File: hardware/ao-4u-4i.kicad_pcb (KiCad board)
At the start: 4 copper layers, 100 x 85 mm, 225 parts, among them J101 TNG-Power-TOP, J102 TNG-Power-BTM, J103 TNG-Data-TOP, J104 TNG-Data-BTM, P102 Debug, P103 PE, P201 INPUT0, P202 INPUT1, P203 INPUT2, P204 INPUT3, Q101 FDS8449, SW101 BOOT, T101 744273222, U101 STM32F070CBT6, U102 AZ1117EH, U103 82400152, U104 TEL10, U105 TLP293, U106 STEF01, U201 DAC8760, U202 DAC8760, U203 ISO7741DWR, U204 DAC8760, U205 DAC8760, U206 TPS560430YDBVR, U207 TPS7A3001DGNR, U208 TPS7A4901DGNR, U209 LTC3261, X101 TBD

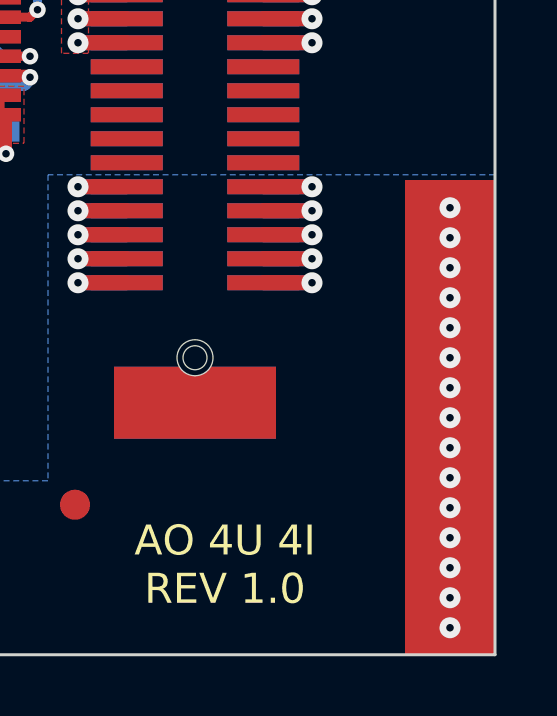
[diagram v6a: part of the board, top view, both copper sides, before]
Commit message: add hook footprint
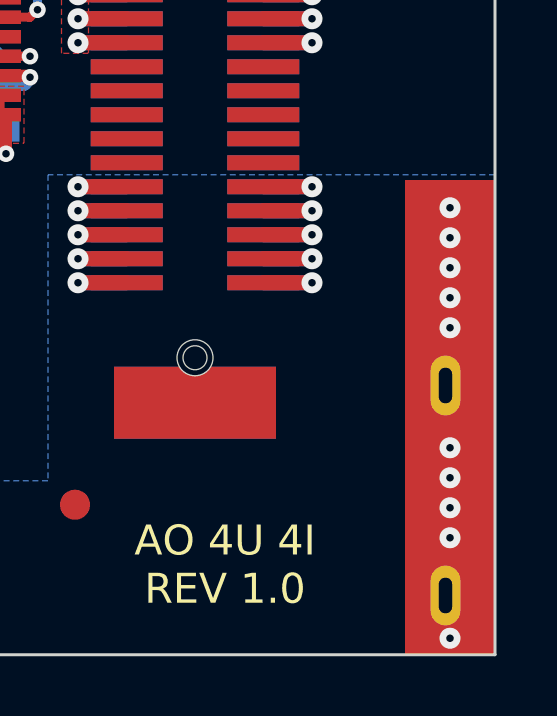
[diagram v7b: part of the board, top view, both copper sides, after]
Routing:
- net Earth: track 54.1 -> 54.5 mm, vias 31 -> 26
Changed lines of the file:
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@@
     (thickness 1.6)
     (drawings 29)
-    (tracks 3141)
+    (tracks 3136)
     (zones 0)
     (modules 225)
@@
     (add_net USB-DPC)
   )
+  (module kicad-libraries:PE_Hook (layer F.Cu)
+    (at 188.3 139.6)
+    (fp_text reference P103 (at 0 0.5) (layer F.Fab)
+      (effects (font (size 0.15 0.15) (thickness 0.0375)))
+    )
+    (fp_text value PE (at 0 -0.5) (layer F.Fab)
+      (effects (font (size 0.15 0.15) (thickness 0.0375)))
+    )
+    (pad 1 thru_hole oval (at -0.15 -1.075) (size 1 2) (drill oval 0.45 1.2) (layers *.Cu *.Mask)
+      (net 12 Earth))
+    (pad 1 thru_hole oval (at -0.15 5.925) (size 1 2) (drill oval 0.45 1.2) (layers *.Cu *.Mask)
+      (net 12 Earth))
+    (pad 1 smd rect (at 0 0) (size 3 15.85) (layers F.Cu)
+      (net 12 Earth))
+    (model Connectors_TF/PE_Hook.wrl
+      (at (xyz 0 0 0))
+      (scale (xyz 1 1 1))
+      (rotate (xyz 0 0 0))
+    )
+  )
   (module LED-LP (layer B.Cu)
     (at 101.4 109 90)
@@
       (clearance 0.65024))
   )
-  (module kicad-libraries:PE_Hook (layer F.Cu)
-    (at 188.3 139.6)
-    (fp_text reference P103 (at 0 0.5) (layer F.Fab)
-      (effects (font (size 0.15 0.15) (thickness 0.0375)))
-    )
-    (fp_text value PE (at 0 -0.5) (layer F.Fab)
-      (effects (font (size 0.15 0.15) (thickness 0.0375)))
-    )
-    (pad 1 smd rect (at 0 0) (size 3 15.85) (layers B.Cu B.Paste B.Mask)
-      (net 12 Earth))
-    (pad 1 smd rect (at 0 0) (size 3 15.85) (layers F.Cu F.Paste F.Mask)
-      (net 12 Earth))
-  )
   (module kicad-libraries:TEL10 (layer F.Cu)
     (at 133.15 135.25 180)
@@
   (via (at 175.9 135.1) (size 0.7) (drill 0.25) (layers F.Cu B.Cu) (net 12))
   (segment (start 175.9 135.1) (end 177.525 135.1) (width 0.5) (layer F.Cu) (net 12) (status 800000))
-  (via (at 188.3 139.6) (size 0.7) (drill 0.25) (layers F.Cu B.Cu) (net 12))
-  (via (at 188.3 138.6) (size 0.7) (drill 0.25) (layers F.Cu B.Cu) (net 12))
   (segment (start 188.3 139.6) (end 188.3 138.6) (width 0.7) (layer F.Cu) (net 12))
-  (via (at 188.3 137.6) (size 0.7) (drill 0.25) (layers F.Cu B.Cu) (net 12))
   (segment (start 188.3 139.6) (end 188.3 137.6) (width 0.7) (layer F.Cu) (net 12))
   (via (at 188.3 136.6) (size 0.7) (drill 0.25) (layers F.Cu B.Cu) (net 12))
@@
   (via (at 188.3 143.6) (size 0.7) (drill 0.25) (layers F.Cu B.Cu) (net 12))
   (segment (start 188.3 142.6) (end 188.3 143.6) (width 0.7) (layer B.Cu) (net 12))
-  (via (at 188.3 144.6) (size 0.7) (drill 0.25) (layers F.Cu B.Cu) (net 12))
   (segment (start 188.3 143.6) (end 188.3 144.6) (width 0.7) (layer F.Cu) (net 12))
-  (via (at 188.3 145.6) (size 0.7) (drill 0.25) (layers F.Cu B.Cu) (net 12))
   (segment (start 188.3 144.6) (end 188.3 145.6) (width 0.7) (layer B.Cu) (net 12))
-  (via (at 188.3 146.6) (size 0.7) (drill 0.25) (layers F.Cu B.Cu) (net 12))
-  (segment (start 188.3 145.6) (end 188.3 146.6) (width 0.7) (layer F.Cu) (net 12))
   (via (at 188.3 135.6) (size 0.7) (drill 0.25) (layers F.Cu B.Cu) (net 12))
   (segment (start 188.3 136.6) (end 188.3 135.6) (width 0.7) (layer B.Cu) (net 12))
@@
   (segment (start 131.5 143.8) (end 132.2 144.5) (width 0.7) (layer F.Cu) (net 12))
   (segment (start 132.2 144.5) (end 132.3 144.5) (width 0.7) (layer F.Cu) (net 12))
+  (segment (start 188.3 145.6) (end 188.3 146.95) (width 0.7) (layer F.Cu) (net 12))
+  (via (at 188.3 146.95) (size 0.7) (drill 0.25) (layers F.Cu B.Cu) (net 12))
   (segment (start 126.60114 141.7999) (end 126.8 141.60104) (width 1) (layer F.Cu) (net 13))
   (segment (start 126.60114 143.6) (end 126.60114 141.7999) (width 1) (layer F.Cu) (net 13))
